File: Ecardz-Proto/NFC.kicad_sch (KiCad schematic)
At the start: 10 parts, among them IC1 M24LR04E-RMN6T/2

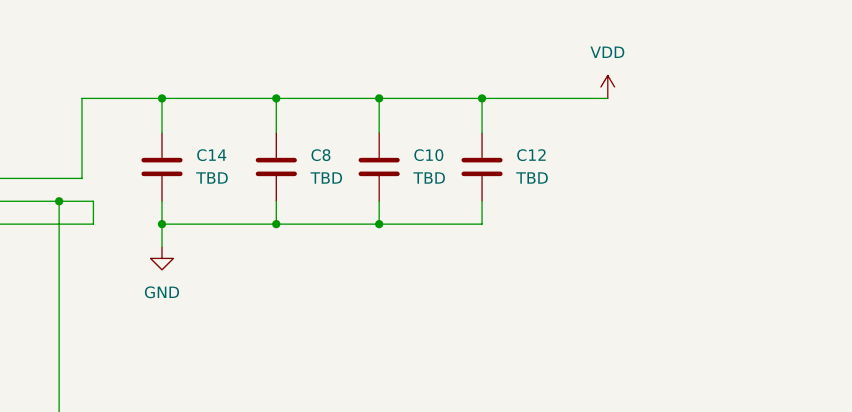
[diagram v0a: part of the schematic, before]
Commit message: added zener and extra cap footprints
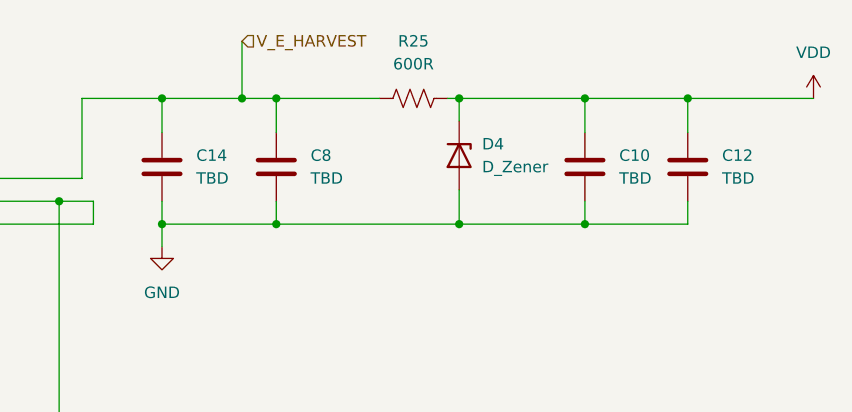
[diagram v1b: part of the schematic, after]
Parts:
- added D4: D_Zener, Diode_SMD:D_SOD-123, symbol Device:D_Zener
- added R25: 600R, Resistor_SMD:R_0603_1608Metric_Pad0.98x0.95mm_HandSolder, symbol Device:R_US
- IC1: MANUFACTURER PART NUMBER (none) -> M24LR04E-RDW6T/2
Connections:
- net GND: now also D4.2 (A)
- net VDD: now also D4.1 (K), R25.2; no longer C14.1, C8.1, IC1.1 (VOUT)
- new net V_E_HARVEST: C14.1, C8.1, IC1.1 (VOUT), R25.1
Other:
- moved on the sheet: C10, C12

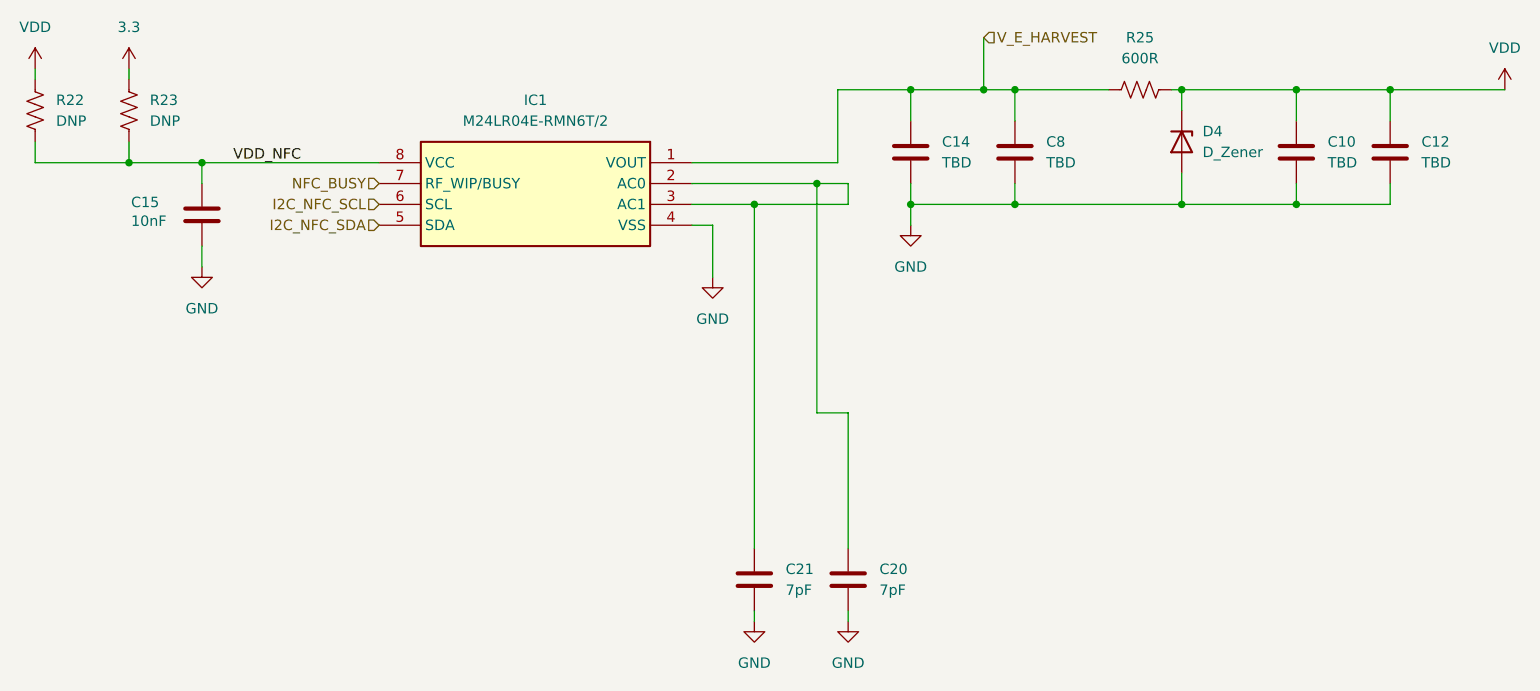
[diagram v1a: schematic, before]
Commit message: added parts numbers for everything
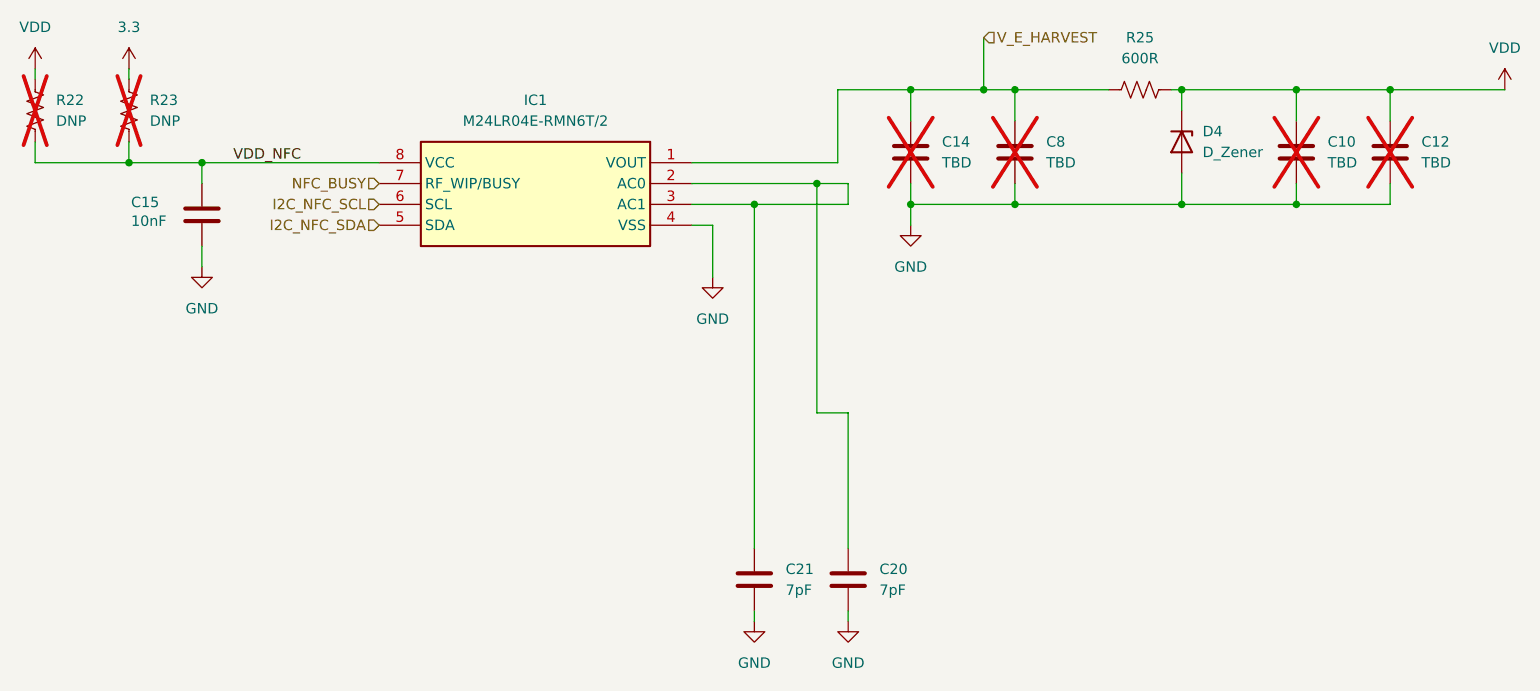
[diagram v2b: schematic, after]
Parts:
- C10, C12, C14, C8, R22, R23: now not fitted
- C15: Digikey Part Number (none) -> 399-C0603C102K5RACTUTR-ND; MANUFACTURER PART NUMBER (none) -> C0603C102K5RACTU
- C20, C21: Digikey Part Number (none) -> 490-13324-2-ND; MANUFACTURER PART NUMBER (none) -> GRM0335C1E7R0CA01D
- D4: Digikey Part Number (none) -> MMSZ4684T1GOSTR-ND
- IC1: Digikey Part Number (none) -> 497-12879-2-ND
- R25: Digikey Part Number (none) -> 541-590HTR-ND
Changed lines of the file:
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@@
 		(in_bom yes)
 		(on_board yes)
-		(dnp no)
+		(dnp yes)
 		(fields_autoplaced yes)
 		(property "Reference" "C12"
@@
 		)
 		(property "Description" "Unpolarized capacitor"
+			(at 262.89 33.02 0)
+			(effects
+				(font
+					(size 1.27 1.27)
+				)
+				(hide yes)
+			)
+		)
+		(property "Digikey Part Number" ""
 			(at 262.89 33.02 0)
 			(effects
@@
 			)
 		)
+		(property "MANUFACTURER PART NUMBER" "C0603C102K5RACTU"
+			(at 118.11 40.64 0)
+			(effects
+				(font
+					(size 1.27 1.27)
+				)
+				(hide yes)
+			)
+		)
+		(property "Digikey Part Number" "399-C0603C102K5RACTUTR-ND"
+			(at 118.11 40.64 0)
+			(effects
+				(font
+					(size 1.27 1.27)
+				)
+				(hide yes)
+			)
+		)
 		(pin "1"
 		)
@@
 		(in_bom yes)
 		(on_board yes)
-		(dnp no)
+		(dnp yes)
 		(property "Reference" "C8"
 			(at 220.98 31.7499 0)
@@
 			)
 		)
+		(property "Digikey Part Number" ""
+			(at 217.17 33.02 0)
+			(effects
+				(font
+					(size 1.27 1.27)
+				)
+				(hide yes)
+			)
+		)
 		(pin "1"
 		)
@@
 		)
 		(property "MANUFACTURER PART NUMBER" "CRCW0603590RFKEA"
+			(at 232.41 25.4 0)
+			(effects
+				(font
+					(size 1.27 1.27)
+				)
+				(hide yes)
+			)
+		)
+		(property "Digikey Part Number" "541-590HTR-ND"
 			(at 232.41 25.4 0)
 			(effects
@@
 			)
 		)
+		(property "MANUFACTURER PART NUMBER" "GRM0335C1E7R0CA01D"
+			(at 185.42 85.09 0)
+			(effects
+				(font
+					(size 1.27 1.27)
+				)
+				(hide yes)
+			)
+		)
+		(property "Digikey Part Number" "490-13324-2-ND"
+			(at 185.42 85.09 0)
+			(effects
+				(font
+					(size 1.27 1.27)
+				)
+				(hide yes)
+			)
+		)
 		(pin "1"
 		)
@@
 			)
 		)
+		(property "Digikey Part Number" "497-12879-2-ND"
+			(at 177.8 34.29 0)
+			(effects
+				(font
+					(size 1.27 1.27)
+				)
+				(hide yes)
+			)
+		)
 		(pin "8"
 		)
@@
 		(in_bom yes)
 		(on_board yes)
-		(dnp no)
+		(dnp yes)
 		(fields_autoplaced yes)
 		(property "Reference" "R22"
@@
 		)
 		(property "Sim.Type" ""
+			(at 97.79 27.94 0)
+			(effects
+				(font
+					(size 1.27 1.27)
+				)
+				(hide yes)
+			)
+		)
+		(property "Digikey Part Number" ""
 			(at 97.79 27.94 0)
 			(effects
@@
 		(in_bom yes)
 		(on_board yes)
-		(dnp no)
+		(dnp yes)
 		(fields_autoplaced yes)
 		(property "Reference" "C14"
@@
 			)
 		)
+		(property "Digikey Part Number" ""
+			(at 204.47 33.02 0)
+			(effects
+				(font
+					(size 1.27 1.27)
+				)
+				(hide yes)
+			)
+		)
 		(pin "1"
 		)
@@
 		(in_bom yes)
 		(on_board yes)
-		(dnp no)
+		(dnp yes)
 		(fields_autoplaced yes)
 		(property "Reference" "R23"
@@
 			)
 		)
+		(property "Digikey Part Number" ""
+			(at 109.22 27.94 0)
+			(effects
+				(font
+					(size 1.27 1.27)
+				)
+				(hide yes)
+			)
+		)
 		(pin "1"
 		)
@@
 		)
 		(property "MANUFACTURER PART NUMBER" "MMSZ4684T1G"
+			(at 237.49 31.75 0)
+			(effects
+				(font
+					(size 1.27 1.27)
+				)
+				(hide yes)
+			)
+		)
+		(property "Digikey Part Number" "MMSZ4684T1GOSTR-ND"
 			(at 237.49 31.75 0)
 			(effects
@@
 			)
 		)
+		(property "MANUFACTURER PART NUMBER" "GRM0335C1E7R0CA01D"
+			(at 196.85 85.09 0)
+			(effects
+				(font
+					(size 1.27 1.27)
+				)
+				(hide yes)
+			)
+		)
+		(property "Digikey Part Number" "490-13324-2-ND"
+			(at 196.85 85.09 0)
+			(effects
+				(font
+					(size 1.27 1.27)
+				)
+				(hide yes)
+			)
+		)
 		(pin "1"
 		)
@@
 		(in_bom yes)
 		(on_board yes)
-		(dnp no)
+		(dnp yes)
 		(fields_autoplaced yes)
 		(property "Reference" "C10"
@@
 			(at 251.46 33.02 0)
 			(effects
+				(font
+					(size 1.27 1.27)
+				)
+				(hide yes)
+			)
+		)
+		(property "Digikey Part Number" ""
+			(at 251.46 33.02 0)
+			(effects
